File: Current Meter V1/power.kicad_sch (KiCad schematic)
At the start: 6 parts, among them J1 USB_C_Receptacle_PowerOnly_6P, U6 AMS1117-3.3

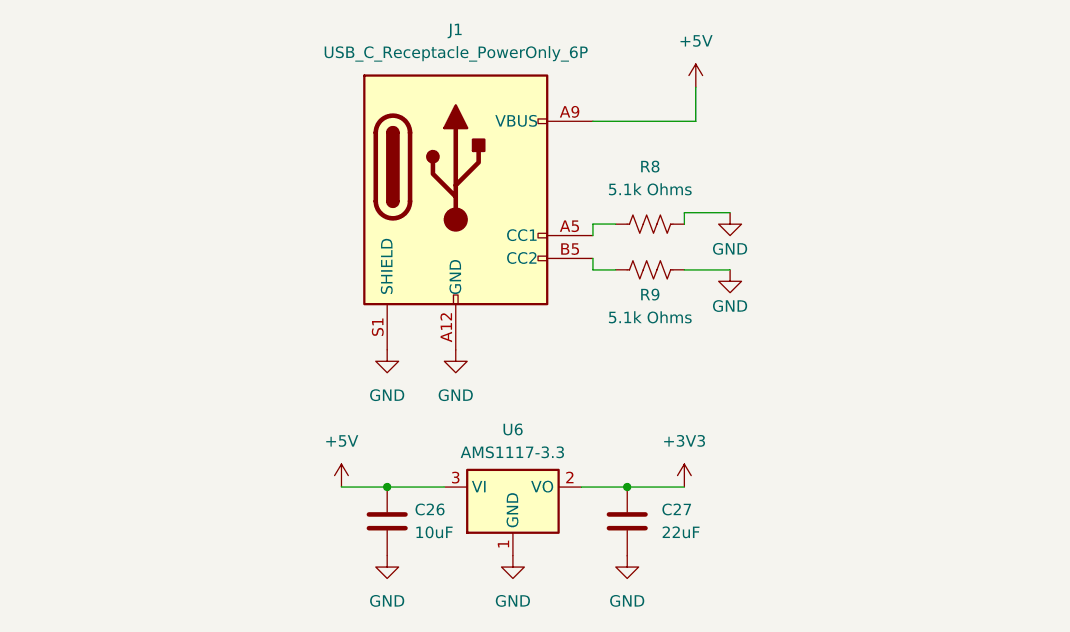
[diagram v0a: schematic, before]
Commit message: Redesign op amp circuit for 0-3.3v output previous design clipped to negative
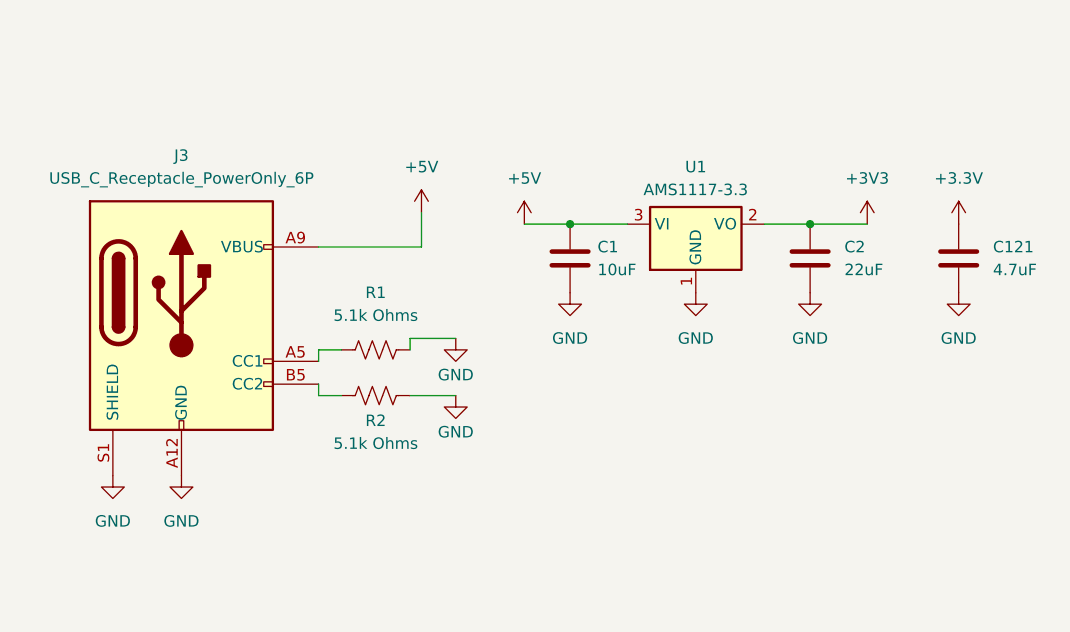
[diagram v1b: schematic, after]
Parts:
- removed J1: USB_C_Receptacle_PowerOnly_6P, symbol Connector:USB_C_Receptacle_PowerOnly_6P
- added C121: 4.7uF, symbol Device:C
- added J3: USB_C_Receptacle_PowerOnly_6P, symbol Connector:USB_C_Receptacle_PowerOnly_6P
- renumbered C26 to C1, C27 to C2, R8 to R1, R9 to R2, U6 to U1
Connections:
- net +5V: now also J3.A9 (VBUS), J3.B9 (VBUS)
- net GND: now also C121.2, J3.A12 (GND), J3.B12 (GND), J3.S1 (SHIELD)
- net at R2.1: now also J3.B5 (CC2)
- net at R1.1: now also J3.A5 (CC1)
- new net +3.3V: C121.1
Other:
- moved on the sheet: C1, C2, R1, R2, U1
